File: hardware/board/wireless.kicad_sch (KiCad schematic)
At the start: 1 part, among them J1 Bus_M.2_Socket_E

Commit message: added stuff
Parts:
- removed J1: Bus_M.2_Socket_E, symbol Connector:Bus_M.2_Socket_E
- added U5: AP6256, lcsc:QFN-44_L12.0-W12.0-P0.90-TL_AP6256, symbol lcsc:AP6256
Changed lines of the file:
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@@
 	(paper "A4")
 	(symbol
-		(lib_id "Connector:Bus_M.2_Socket_E")
-		(at 219.71 90.17 0)
+		(lib_id "lcsc:AP6256")
+		(at 247.65 86.36 0)
 		(unit 1)
 		(exclude_from_sim no)
@@
 		(dnp no)
 		(fields_autoplaced yes)
-		(property "Reference" "J1"
-			(at 221.8533 39.37 0)
+		(property "Reference" "U5"
+			(at 247.65 49.53 0)
 			(effects
 				(font
 					(size 1.27 1.27)
 				)
-				(justify left)
 			)
 		)
-		(property "Value" "Bus_M.2_Socket_E"
-			(at 221.8533 41.91 0)
+		(property "Value" "AP6256"
+			(at 247.65 52.07 0)
 			(effects
 				(font
 					(size 1.27 1.27)
 				)
-				(justify left)
 			)
 		)
-		(property "Footprint" ""
-			(at 219.71 63.5 0)
+		(property "Footprint" "lcsc:QFN-44_L12.0-W12.0-P0.90-TL_AP6256"
+			(at 247.65 123.19 0)
 			(effects
 				(font
@@
 			)
 		)
-		(property "Datasheet" "https://web.archive.org/web/20200613074028/http://read.pudn.com/downloads794/doc/project/3133918/PCIe_M.2_Electromechanical_Spec_Rev1.0_Final_11012013_RS_Clean.pdf#page=150"
-			(at 219.71 77.47 0)
+		(property "Datasheet" ""
+			(at 247.65 86.36 0)
 			(effects
 				(font
@@
 			)
 		)
-		(property "Description" "M.2 Socket 1-SD Mechanical Key E"
-			(at 219.71 90.17 0)
+		(property "Description" ""
+			(at 247.65 86.36 0)
 			(effects
 				(font
@@
 			)
 		)
-		(pin "51"
+		(property "LCSC Part" "C5248079"
+			(at 247.65 125.73 0)
+			(effects
+				(font
+					(size 1.27 1.27)
+				)
+				(hide yes)
+			)
 		)
-		(pin "62"
+		(pin "28"
+		)
+		(pin "2"
+		)
+		(pin "3"
+		)
+		(pin "46"
+		)
+		(pin "38"
+		)
+		(pin "27"
+		)
+		(pin "43"
+		)
+		(pin "32"
+		)
+		(pin "10"
+		)
+		(pin "47"
+		)
+		(pin "4"
+		)
+		(pin "13"
+		)
+		(pin "37"
+		)
+		(pin "42"
+		)
+		(pin "44"
+		)
+		(pin "16"
+		)
+		(pin "9"
+		)
+		(pin "14"
+		)
+		(pin "22"
 		)
 		(pin "39"
 		)
-		(pin "69"
+		(pin "35"
 		)
-		(pin "41"
+		(pin "30"
 		)
-		(pin "66"
+		(pin "6"
 		)
-		(pin "67"
+		(pin "33"
+		)
+		(pin "1"
+		)
+		(pin "5"
+		)
+		(pin "26"
+		)
+		(pin "7"
+		)
+		(pin "12"
+		)
+		(pin "11"
 		)
 		(pin "17"
 		)
-		(pin "75"
+		(pin "18"
 		)
-		(pin "61"
+		(pin "40"
 		)
-		(pin "73"
+		(pin "15"
 		)
-		(pin "58"
+		(pin "20"
 		)
-		(pin "6"
+		(pin "19"
 		)
-		(pin "3"
+		(pin "31"
 		)
-		(pin "37"
+		(pin "34"
 		)
-		(pin "59"
+		(pin "24"
 		)
-		(pin "55"
-		)
-		(pin "13"
-		)
-		(pin "49"
+		(pin "8"
 		)
 		(pin "21"
@@
 		(pin "23"
 		)
-		(pin "35"
-		)
-		(pin "43"
-		)
-		(pin "68"
-		)
-		(pin "5"
-		)
-		(pin "15"
-		)
-		(pin "19"
-		)
-		(pin "47"
-		)
-		(pin "4"
-		)
-		(pin "74"
-		)
-		(pin "1"
-		)
-		(pin "52"
-		)
-		(pin "2"
-		)
-		(pin "18"
-		)
-		(pin "33"
-		)
-		(pin "70"
-		)
 		(pin "45"
 		)
-		(pin "63"
-		)
-		(pin "11"
-		)
-		(pin "65"
-		)
-		(pin "9"
-		)
-		(pin "7"
-		)
-		(pin "64"
-		)
-		(pin "38"
-		)
-		(pin "40"
-		)
-		(pin "57"
-		)
-		(pin "42"
-		)
-		(pin "53"
-		)
-		(pin "72"
-		)
-		(pin "71"
-		)
-		(pin "60"
-		)
-		(pin "56"
-		)
-		(pin "8"
-		)
-		(pin "10"
-		)
-		(pin "54"
-		)
-		(pin "12"
-		)
-		(pin "14"
-		)
-		(pin "22"
-		)
-		(pin "32"
-		)
-		(pin "34"
-		)
-		(pin "20"
+		(pin "41"
 		)
 		(pin "36"
 		)
-		(pin "16"
+		(pin "29"
 		)
-		(pin "50"
-		)
-		(pin "44"
-		)
-		(pin "48"
-		)
-		(pin "46"
+		(pin "25"
 		)
 		(instances
-			(project "frost"
+			(project ""
 				(path "/3bc38516-4fe0-4022-adb8-9fd55b66cd2d/8c9baa61-05fe-4ea8-9287-072748c6c20c"
-					(reference "J1")
+					(reference "U5")
 					(unit 1)
 				)

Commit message: start of ethernet
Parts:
- removed U5: AP6256, lcsc:QFN-44_L12.0-W12.0-P0.90-TL_AP6256, symbol lcsc:AP6256
- added C156: 22uF X5R 10V, Capacitor_SMD:C_0805_2012Metric, symbol Device:C
- added C157, C162: 100nF X5R 10V, Capacitor_SMD:C_0402_1005Metric, symbol Device:C
- added C158, C159: 20pF C0G 50V, Capacitor_SMD:C_0402_1005Metric, symbol Device:C
- added C160, C161, C163: 4.7uF X5R 10V, Capacitor_SMD:C_0603_1608Metric, symbol Device:C
- added C164, C165: 100pF X5R 25V, Capacitor_SMD:C_0201_0603Metric, symbol Device:C
- added C166, C167, C168, C169: 100nF X5R 10V, Capacitor_SMD:C_0201_0603Metric, symbol Device:C
- added C170, C171, C172, C173, C174, C175: DNP, Capacitor_SMD:C_0402_1005Metric, symbol Device:C
- added C176: 10pF C0G 50V, Capacitor_SMD:C_0201_0603Metric, symbol Device:C
- added R92, R93: 22R 5%, Resistor_SMD:R_0402_1005Metric, symbol Device:R
- added R94: 0R 5%, Resistor_SMD:R_0402_1005Metric, symbol Device:R
- added R95, R96, R97, R99: 0R 5%, Resistor_SMD:R_0603_1608Metric, symbol Device:R
- added R98: 10K 5%, Resistor_SMD:R_0402_1005Metric, symbol Device:R
- added RF1, RF2, RF3: BWIPX-1-001E, lcsc:IPEX-SMD_BWIPX-1-001E, symbol lcsc:BWIPX-1-001E
- added U34: AP6275PR3, lcsc:WIRELM-SMD_AMPAK_AP6275P, symbol lcsc:AP6275PR3
- added U35, U5: TFM252012ALVA2R2MTAA, lcsc:L1008, symbol lcsc:TFM252012ALVA2R2MTAA
- added X3: S3237400121040, lcsc:CRYSTAL-SMD_4P-L3.2-W2.5-BL, symbol lcsc:S3237400121040
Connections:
- new net: C174.1, C176.2, U34.48 (NC)
- new net: C172.1, R96.2, RF1.1 (SIG)
- new net: U34.26 (CSR_VLX), U5.1
- new net: C160.1, U34.25 (CBUCK_0P9), U5.2
- new net: C175.1, C176.1, RF3.1 (SIG)
- new net: C165.2, U34.33 (PCIE_RCLK_N)
- new net: C164.2, U34.35 (PCIE_RCLK_P)
- new net: C166.2, U34.44 (PCIE_RX_N)
- new net: C171.1, R95.2, RF2.1 (SIG)
- new net: C159.1, U34.13 (XTAL_XOP), X3.3 (OSC2)
- new net: C158.1, R99.2, X3.1 (OSC1)
- new net: R99.1, U34.14 (XTAL_XON)
- new net: U34.28 (ASR_VLX), U35.1
- new net: C161.1, U34.29 (ABUCK_1P12), U35.2
- new net: C170.1, R95.1, U34.2 (WL_ANT0)
- new net: C169.2, U34.47 (PCIE_TX_P)
- new net: C173.1, R96.1, U34.9 (WL_ANT1)
- new net: C167.2, U34.45 (PCIE_RX_P)
- new net: C168.2, U34.46 (PCIE_TX_N)
- new net BT_REG_ON_H_GPIO0_C1: U34.38 (BT_REG_ON)
- new net BT_WAKE_HOST_H_GPIO0_B7: U34.50 (BT_HOST_WAKE)
- new net GND: C156.2, C157.2, C158.2, C159.2, C160.2, C161.2, C162.2, C163.2, C170.2, C171.2, C172.2, C173.2, C174.2, C175.2, RF1.2 (GND), RF1.3 (GND), RF2.2 (GND), RF2.3 (GND), RF3.2 (GND), RF3.3 (GND), U34.1 (GND), U34.10 (GND), U34.11 (GND), U34.23 (GND), U34.27 (GND), U34.3 (GND), U34.30 (GND), U34.32 (GND), U34.39 (GND), U34.4 (GND), U34.5 (GND), U34.6 (GND), U34.7 (GND), U34.8 (GND), X3.2 (GND), X3.4 (GND)
- new net HOST_WAKE_BT_H_GPIO0_B0: U34.49 (BT_WAKE)
- new net PCIE20_CLKREQn_1V8: R92.1, U34.37 (PCIE_CLKREQ_L)
- new net PCIE20_CLKREQn_M1: R92.2
- new net PCIE20_PERSTn_1V8: R94.1, U34.12 (PCIE_PREST_L)
- new net PCIE20_PERSTn_M1: R94.2
- new net PCIE20_REFCLKN: C165.1
- new net PCIE20_REFCLKP: C164.1
- new net PCIE20_RXN: C168.1
- new net PCIE20_RXP: C169.1
- new net PCIE20_TXN: C166.1
- new net PCIE20_TXP: C167.1
- new net PCIE20_WAKEn_1V8: R93.1, U34.24 (PCIE_PME_L)
- new net PCIE20_WAKEn_M1: R93.2
- new net PMIC_32KOUT_WIFI: R98.2, U34.31 (LPO_IN)
- new net SOC_PCM_CLK: U34.22 (BT_PCM_CLK)
- new net SOC_PCM_IN: U34.19 (BT_PCM_OUT)
- new net SOC_PCM_OUT: U34.20 (BT_PCM_IN)
- new net SOC_PCM_SYNC: U34.21 (BT_PCM_SYNC)
- new net UART1_CTSn_M0: U34.42 (BT_UART_RTS_N)
- new net UART1_RTSn_M0: U34.43 (BT_UART_CTS_N)
- new net UART1_RX_M0: U34.40 (BT_UART_TXD), U34.41 (BT_UART_RXD)
- new net VCC3V3_SYS: R97.2
- new net VCCIO_WL: C162.1, C163.1, U34.34 (VDDIO)
- new net VCC_WL: C156.1, C157.1, R97.1, R98.1, U34.36 (VBAT)
- new net WIFI_REG_ON_H_GPIO0_C0: U34.15 (WL_REG_ON)
- new net WIFI_WAKE_HOST_H_GPIO0_C4: U34.16 (WL_HOST_WAKE)
- no-connect marks 0 -> 2
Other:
- note added: "Close to VBAT pin (36)"
- note added: "Close to VDDIO pin (34)"

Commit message: aaa
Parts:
- R99: footprint Resistor_SMD:R_0603_1608Metric -> Resistor_SMD:R_0402_1005Metric
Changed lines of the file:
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@@
 			)
 		)
-		(property "Footprint" "Resistor_SMD:R_0603_1608Metric"
+		(property "Footprint" "Resistor_SMD:R_0402_1005Metric"
 			(at 86.36 93.218 90)
 			(effects

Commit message: finished schematic!
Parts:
- added C351: 100nF X5R 10V, Capacitor_SMD:C_0201_0603Metric, symbol Device:C
- added U1: RK3568, RK3568:BGA636C65P28X28_1900X1900X168, symbol RK3568:RK3568
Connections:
- net GND: now also C351.2
- net SOC_PCM_CLK: now also U1.F25 (GPIO2_C2_D)
- net SOC_PCM_IN: now also U1.F26 (GPIO2_C5_D)
- net SOC_PCM_OUT: now also U1.H23 (GPIO2_C4_D)
- net SOC_PCM_SYNC: now also U1.H24 (GPIO2_C3_D)
- net UART1_CTSn_M0: now also U1.F27 (GPIO2_B6_U)
- net UART1_RTSn_M0: now also U1.G28 (GPIO2_B5_U)
- net UART1_RX_M0: now also U1.F28 (GPIO2_B3_U)
- net VCCIO_WL: now also C351.1, U1.J21 (VCCIO4)
- new net UART1_TX_M0: U1.G27 (GPIO2_B4_U)
- no-connect marks 2 -> 14
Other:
- note added: "WiFi / Bluetooth"

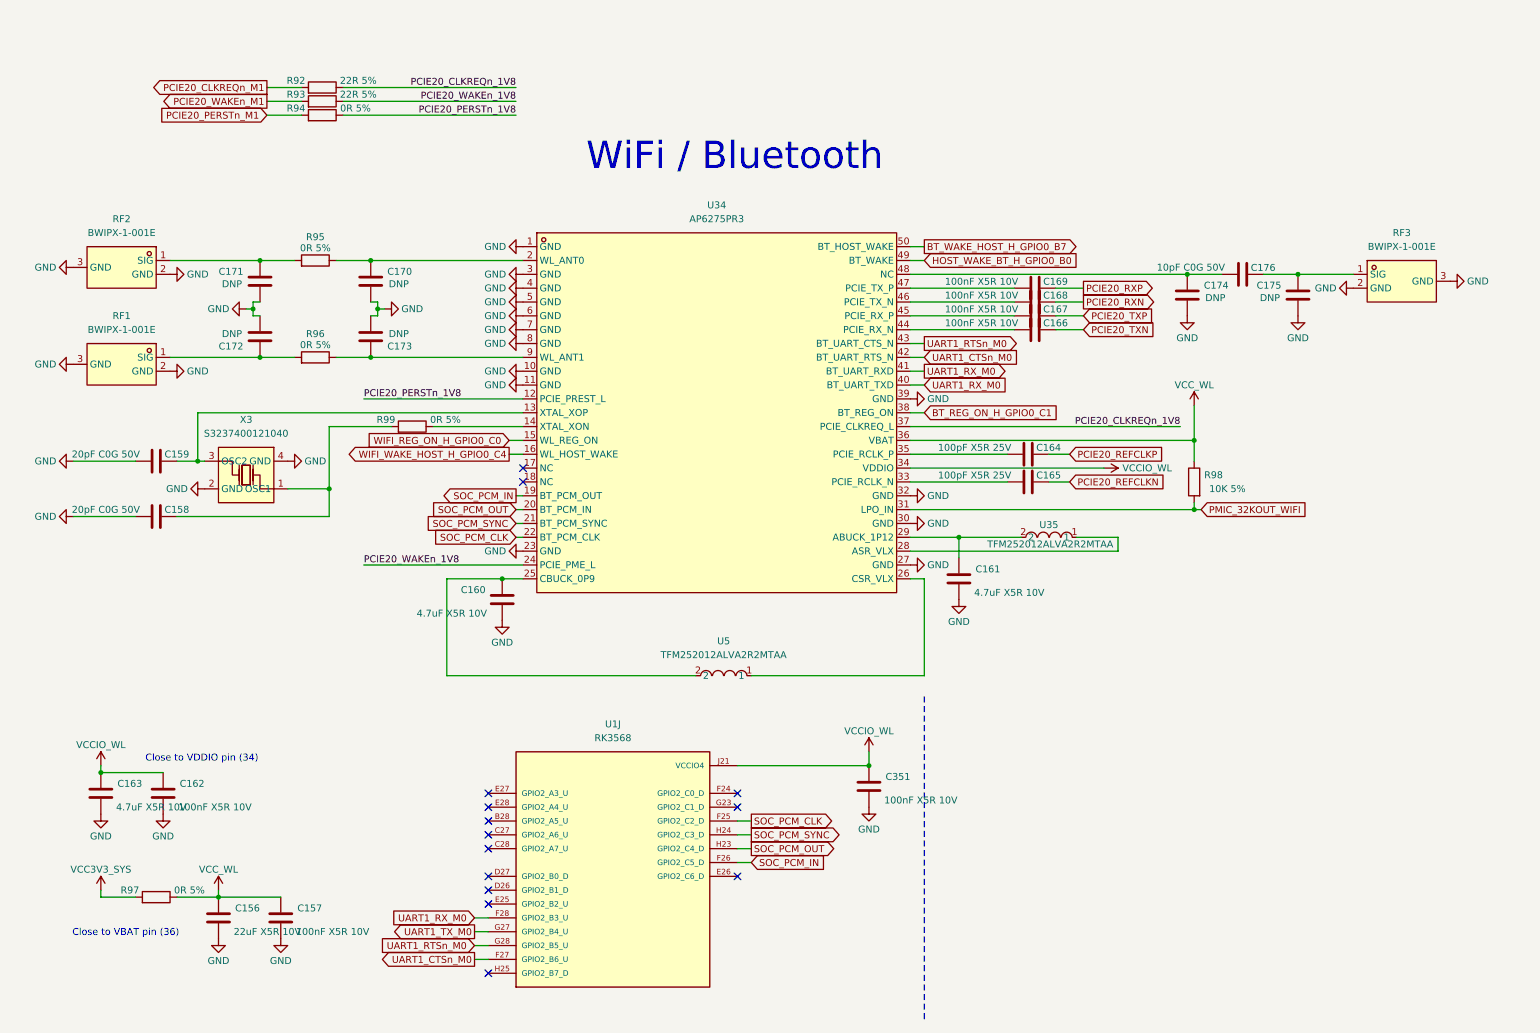
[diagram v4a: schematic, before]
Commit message: finished beautifying schematic
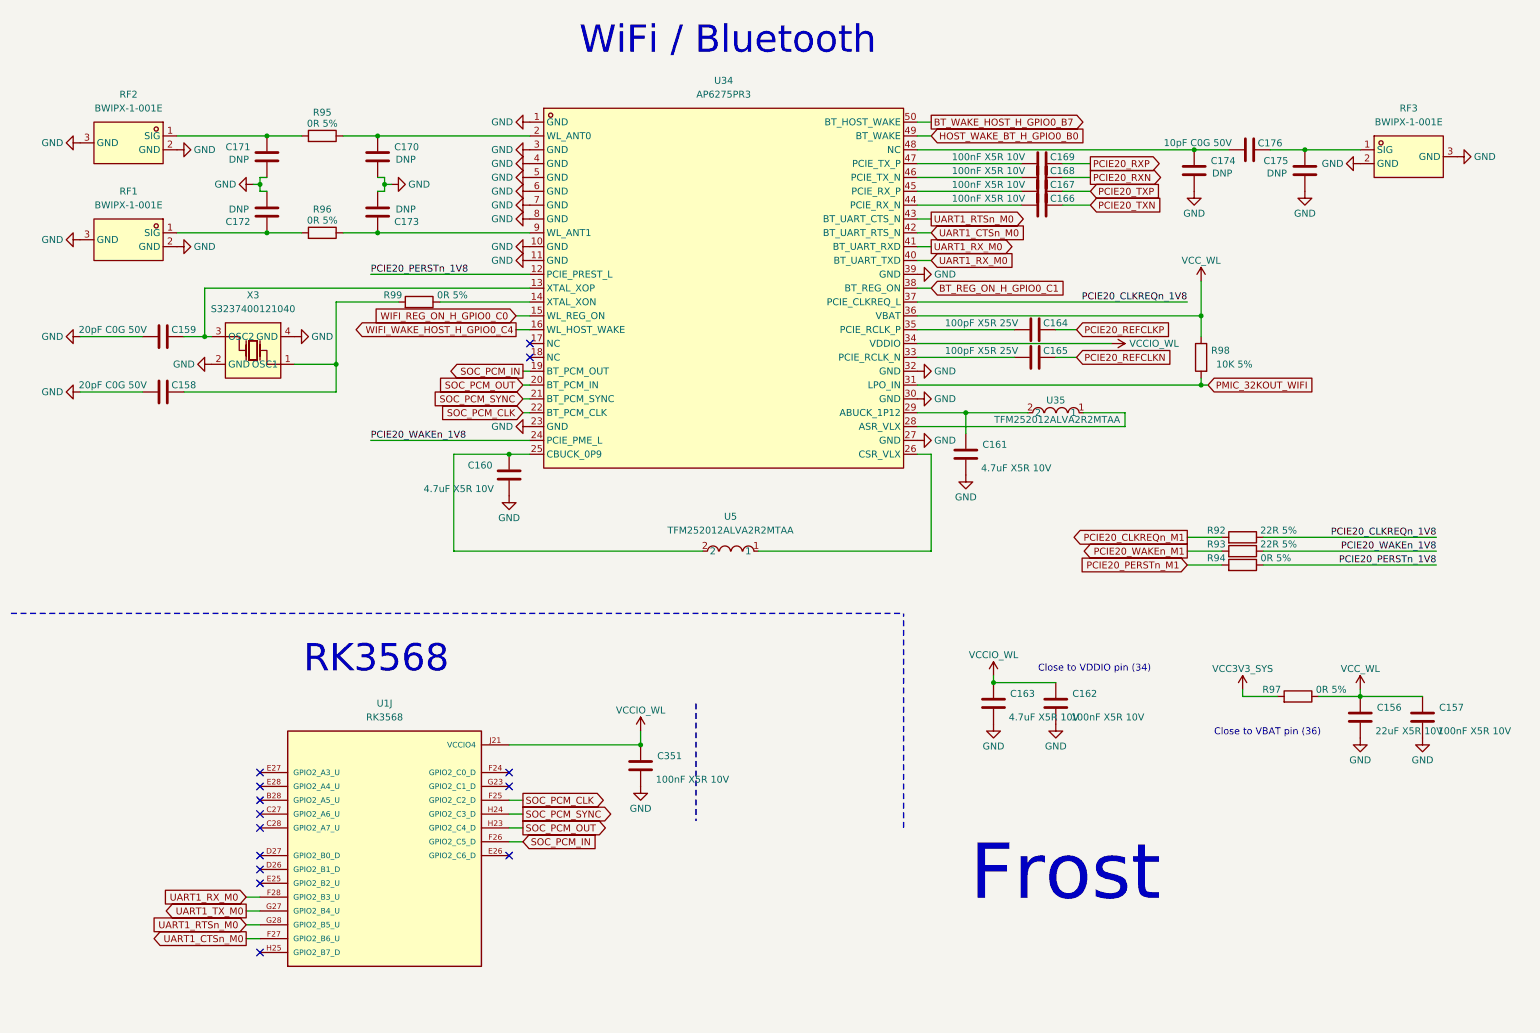
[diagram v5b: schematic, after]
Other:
- note added: "Frost"
- note added: "RK3568"
- moved on the sheet: C156, C157, C158, C159, C160, C161, C162, C163, C164, C165, C166, C167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

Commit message: did a thing
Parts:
- R94: value 0R 5% -> 22R 5%
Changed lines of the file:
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@@
 			)
 		)
-		(property "Value" "0R 5%"
-			(at 244.856 115.57 90)
+		(property "Value" "22R 5%"
+			(at 245.364 115.57 90)
 			(effects
 				(font
